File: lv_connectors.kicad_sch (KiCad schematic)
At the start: 18 parts, among them J2 Conn_01x04, J3 Conn_01x04, J4 Conn_01x04, J6 Conn_01x02, J7 Conn_01x04, J8 Conn_01x08, J9 Conn_01x02, U15 ADP121-AUJZ33R7, U2 L7805, U24 SN74LVC1G00DBV

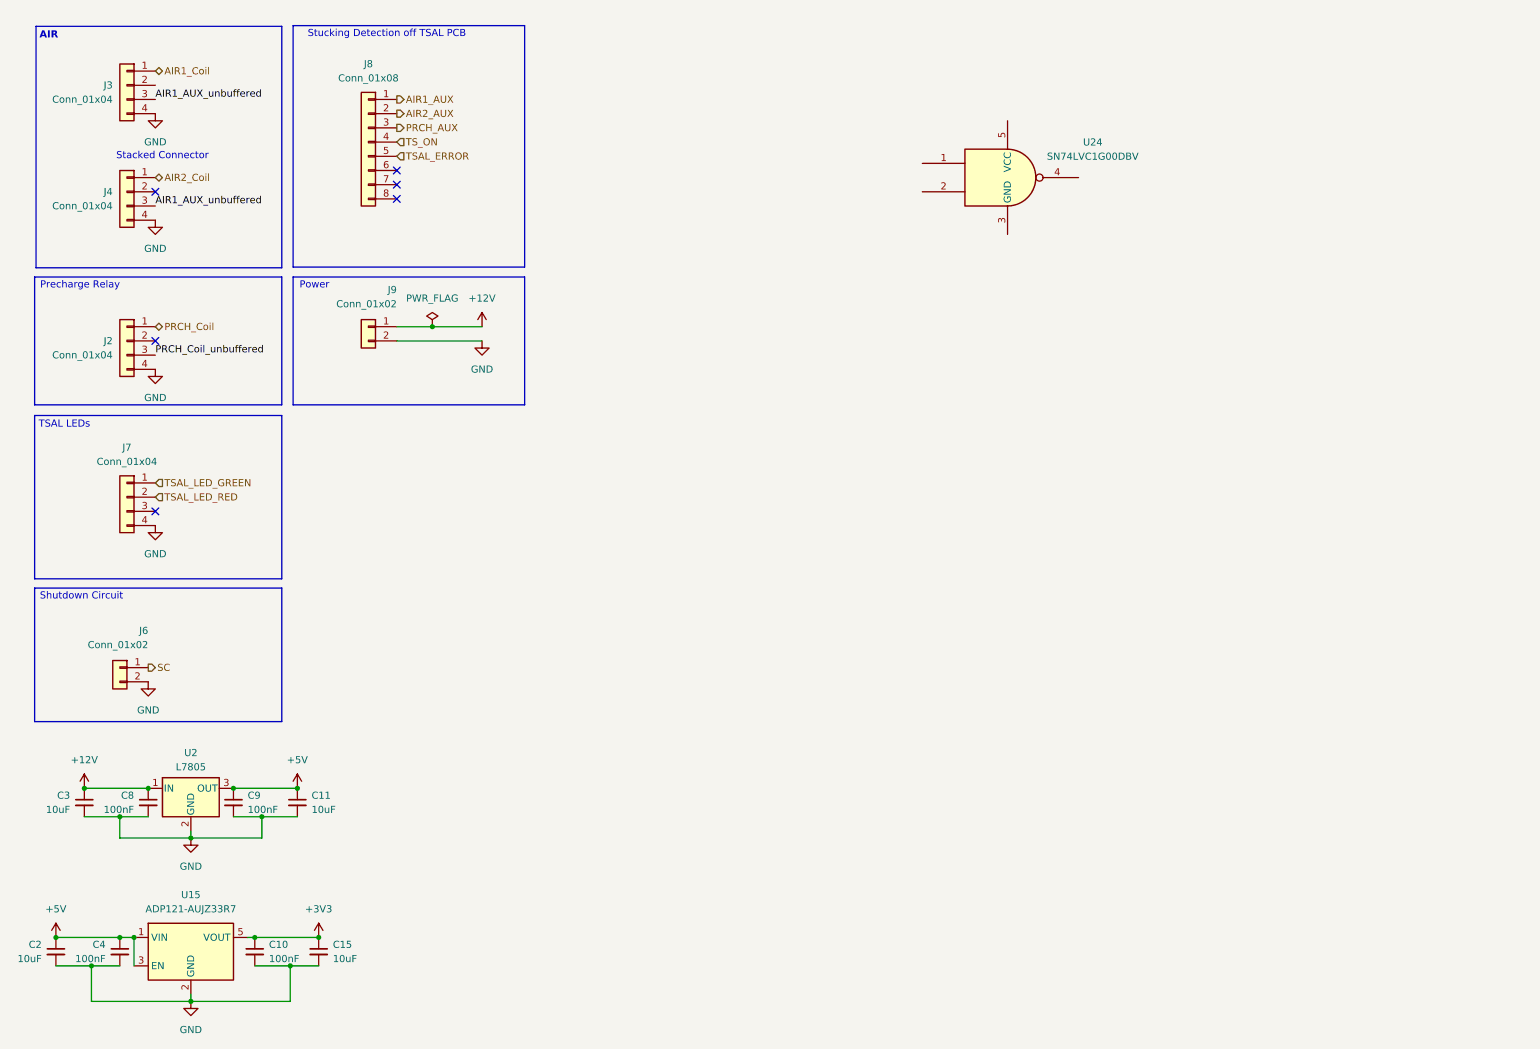
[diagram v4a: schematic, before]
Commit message: Added decoupling Caps
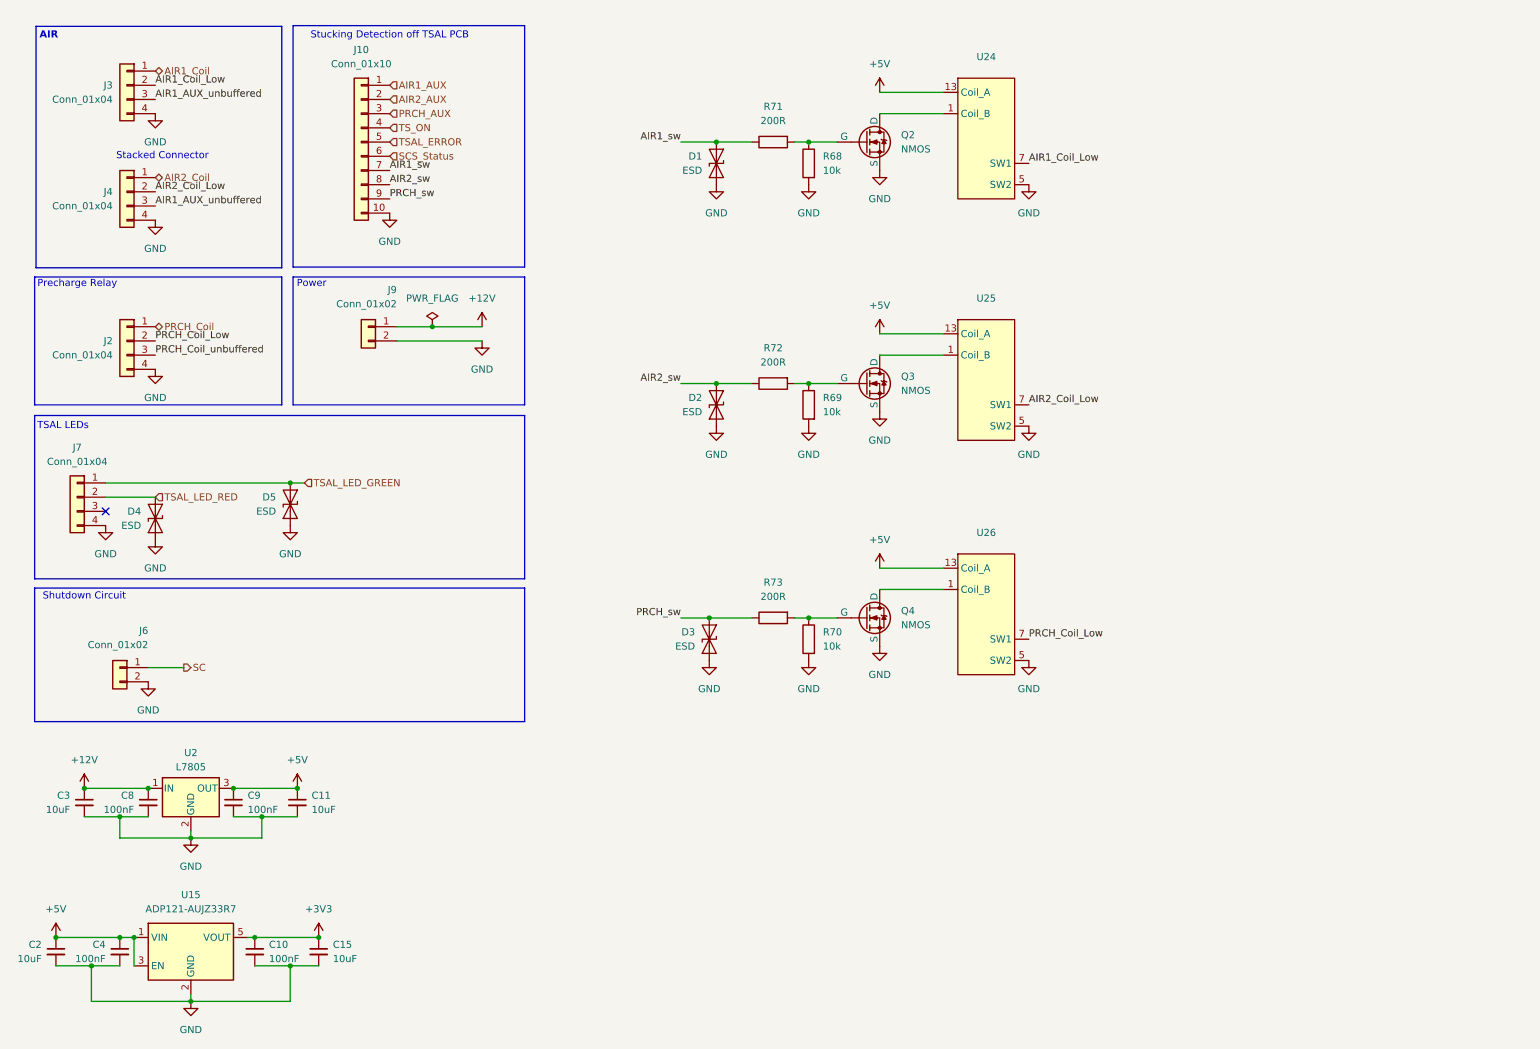
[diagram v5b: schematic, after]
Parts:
- removed J8: Conn_01x08, symbol Connector_Generic:Conn_01x08
- removed U24: SN74LVC1G00DBV, Package_TO_SOT_SMD:SOT-23-5, symbol 74xGxx:SN74LVC1G00DBV
- added D1, D2, D3, D4, D5: ESD, Diode_SMD:Infineon_SG-WLL-2-3_0.58x0.28_P0.36mm, symbol Diode:ESD131-B1-W0201
- added J10: Conn_01x10, symbol Connector_Generic:Conn_01x10
- added Q2, Q3, Q4: NMOS, symbol Simulation_SPICE:NMOS
- added R68, R69, R70: 10k, symbol Device:R
- added R71, R72, R73: 200R, symbol Device:R
- added U24, U25, U26: ~, symbol Zettler:AZ9371
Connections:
- net +5V: now also U24.13 (Coil_A), U25.13 (Coil_A), U26.13 (Coil_A)
- net AIR1_AUX: now also J10.1 (Pin_1)
- net AIR2_AUX: now also J10.2 (Pin_2)
- net GND: now also D1.1 (A1), D2.1 (A1), D3.1 (A1), D4.1 (A1), D5.1 (A1), J10.10 (Pin_10), Q2.3 (S), Q3.3 (S), Q4.3 (S), R68.2, R69.2, R70.2, U24.5 (SW2), U25.5 (SW2), U26.5 (SW2)
- net PRCH_AUX: now also J10.3 (Pin_3)
- net TSAL_ERROR: now also J10.5 (Pin_5)
- net TSAL_LED_GREEN: now also D5.2 (A2)
- net TSAL_LED_RED: now also D4.2 (A2)
- net TS_ON: now also J10.4 (Pin_4)
- net AIR1_Coil_Low: now reaches J3.2 (Pin_2)
- net AIR1_Coil_Low: now also U24.7 (SW1)
- net AIR2_Coil_Low: now reaches J4.2 (Pin_2)
- net AIR2_Coil_Low: now also U25.7 (SW1)
- net PRCH_Coil_Low: now reaches J2.2 (Pin_2)
- net PRCH_Coil_Low: now also U26.7 (SW1)
- new net: Q4.1 (D), U26.1 (Coil_B)
- new net: Q4.2 (G), R70.1, R73.2
- new net: Q3.2 (G), R69.1, R72.2
- new net: Q2.1 (D), U24.1 (Coil_B)
- new net: Q2.2 (G), R68.1, R71.2
- new net: Q3.1 (D), U25.1 (Coil_B)
- new net AIR1_sw: D1.2 (A2), J10.7 (Pin_7), R71.1
- new net AIR2_sw: D2.2 (A2), J10.8 (Pin_8), R72.1
- new net PRCH_sw: D3.2 (A2), J10.9 (Pin_9), R73.1
- new net SCS_Status: J10.6 (Pin_6)
- no-connect marks 6 -> 1
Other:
- moved on the sheet: J7

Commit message: Added Rules
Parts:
- removed C10, C4: 100nF, Capacitor_SMD:C_0603_1608Metric, symbol Device:C_Small
- removed C15, C2: 10uF, Capacitor_SMD:C_0603_1608Metric, symbol Device:C_Small
- removed U15: ADP121-AUJZ33R7, Package_TO_SOT_SMD:TSOT-23-5, symbol Regulator_Linear:ADP7142AUJZ-3.3
- added Q5, Q6: PMOS, symbol Simulation_SPICE:PMOS
- added R78, R79: 200R, symbol Device:R
- added R80, R81: 10k, symbol Device:R
- added R85: 30k, symbol Device:R
- added R86: 7k5, symbol Device:R
- U2: Cost 0,958 -> 0,949; Mouser 511-L7805ACD2T-TR -> 511-L7805ABD2T-TR
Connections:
- net AIR1_Coil_Low is gone; now on net AIR1_Coil: J3.2 (Pin_2), U24.7 (SW1)
- net AIR2_Coil_Low is gone; now on net AIR2_Coil: J4.2 (Pin_2), U25.7 (SW1)
- net PRCH_Coil_Low is gone; now on net PRCH_Coil: J2.2 (Pin_2), U26.7 (SW1)
- net AIR1_AUX_unbuffered: no longer J4.3 (Pin_3)
- net AIR1_Coil: no longer J3.1 (Pin_1)
- net AIR2_Coil: no longer J4.1 (Pin_1)
- net GND: now also R86.2
- net PRCH_Coil: no longer J2.1 (Pin_1)
- net SC: now also R85.2, R86.1; no longer J6.1 (Pin_1)
- net TSAL_LED_GREEN: now also R78.1; no longer D5.2 (A2), J7.1 (Pin_1)
- net TSAL_LED_RED: now also R79.1; no longer D4.2 (A2), J7.2 (Pin_2)
- net +12V renamed +24V
- net +24V: now also Q5.1 (D), Q6.1 (D), R80.1, R81.1
- net PRCH_Coil_unbuffered renamed PRCH_AUX_unbuffered
- new net: Q5.2 (G), R78.2, R81.2
- new net: D4.2 (A2), J7.2 (Pin_2), Q6.3 (S)
- new net: D5.2 (A2), J7.1 (Pin_1), Q5.3 (S)
- new net: Q6.2 (G), R79.2, R80.2
- new net AIR2_AUX_unbuffered: J4.3 (Pin_3)
- new net SDC: J2.1 (Pin_1), J3.1 (Pin_1), J4.1 (Pin_1), J6.1 (Pin_1), R85.1
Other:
- note added: "Stucking Detection off PCB"
- note removed: "Stacked Connector"
- note removed: "Stucking Detection off TSAL PCB"
- moved on the sheet: C11, C3, C8, C9, D1, D2, D3, D5, J10, J6, J7, J9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

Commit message: Submission Ready. ESF 15.07.24
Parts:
- removed D1, D2, D3: ESD, Diode_SMD:Infineon_SG-WLL-2-3_0.58x0.28_P0.36mm, symbol Diode:ESD131-B1-W0201
- removed Q2, Q3, Q4: NMOS, symbol Simulation_SPICE:NMOS
- removed R68, R69, R70: 10k, symbol Device:R
- removed R71, R72, R73: 200R, symbol Device:R
- removed U24, U25, U26: ~, symbol Zettler:AZ9371
- added C1, C10: 100nF, symbol Device:C
- added C15, C4: 10uF, symbol Device:C_Polarized
- added R29, R30, R31: 10k, symbol Device:R
- added U15: TBA1-1211E, Converter_DCDC:Converter_DCDC_TRACO_TBA1-xxxxE_Single_THT, symbol Converter_DCDC:TBA1-1211E
- added U18: IP4252CZ16, Package_SON:Nexperia_HUSON-16_USON-16-1EP_1.35x3.3mm_P0.4mm_EP0.4x2.8mm, symbol Power_Protection:IP4252CZ16
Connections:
- net AIR1_AUX_unbuffered is gone; now on net AIR1_AUX: J3.3 (Pin_3)
- net AIR2_AUX_unbuffered is gone; now on net AIR2_AUX: J4.3 (Pin_3)
- net PRCH_AUX_unbuffered is gone; now on net PRCH_AUX: J2.3 (Pin_3)
- net +24V: now also C1.1, C4.1, U15.1 (+Vin); no longer C3.1, C8.1, U2.1 (IN)
- net +5V: now also R29.1, R30.1, R31.1
- net AIR1_AUX: now also R29.2, U18.16 (CH1); no longer J10.1 (Pin_1)
- net AIR2_AUX: now also R30.2, U18.15 (CH2); no longer J10.2 (Pin_2)
- net GND: now also J10.1 (Pin_1), C1.2, C10.2, C15.2, C4.2, U15.2 (-Vin), U15.4 (-Vout), U18.17 (GND)
- net PRCH_AUX: now also R31.2, U18.14 (CH3); no longer J10.3 (Pin_3)
- net TSAL_ERROR: now also U18.12 (CH5); no longer J10.5 (Pin_5)
- net TS_ON: now also U18.13 (CH4); no longer J10.4 (Pin_4)
- net AIR1_sw: no longer names the net of J10.7 (Pin_7)
- net AIR1_sw: now also U18.6 (CH6)
- net AIR2_sw: no longer names the net of J10.8 (Pin_8)
- net AIR2_sw: now also U18.7 (CH7)
- net PRCH_sw: no longer names the net of J10.9 (Pin_9)
- net PRCH_sw: now also U18.8 (CH8)
- net SCS_Status: no longer names the net of J10.6 (Pin_6)
- net SCS_Status: now also U18.5 (CH5)
- new net: J10.2 (Pin_2), U18.1 (CH1)
- new net: J10.3 (Pin_3), U18.2 (CH2)
- new net: J10.4 (Pin_4), U18.3 (CH3)
- new net: J10.5 (Pin_5), U18.4 (CH4)
- new net +9V: C10.1, C15.1, C3.1, C8.1, U15.6 (+Vout), U2.1 (IN)
- new net AIR1_SW: U18.11 (CH6)
- new net AIR2_SW: U18.10 (CH7)
- new net PRCH_SW: U18.9 (CH8)
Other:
- note added: "5V Supply"
- note added: "DC-DC Converter"
- note added: "Power In"
- note removed: "Power"
- moved on the sheet: C11, C3, C8, C9, D4, D5, J10, J2, J3, J4, J6, J7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

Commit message: ⠀⠀⠀⠀⠀⠀⠀⠀⠀⠀⠀⠀⠀⠀⠀⠀⠀⠀⠀⠀⠀⠀⠀⠀⠀⠀⠀⠀⠀⠀⠀⠀⠀⠀⠀⠀⠀⣠⣤⣤⣤⡀⠀⠀⠀⠀⠀⠀⠀⠀⠀⠀⠀⠀⠀⠀⠀⠀⠀⠀⠀⠀⠀⠀⠀ ⠀⠀⠀⠀⠀⠀⠀⠀⠀⠀⠀⠀⠀⠀⠀⠀⠀⠀⠀⠀⠀⠀⠀⠀⠀⠀⠀⠀⠀⠀⠀⠀⠀⠀⣠⣶⣿⠟⠉⠉⠻⣿⡄⠀⠀⠀⠀⠀⠀⠀⠀⠀⠀⠀⠀⠀⠀⠀⠀⠀⠀⠀⠀⠀⠀ ⠀⠀⠀⠀⠀⠀⠀⠀⠀⠀⠀⠀⠀⠀⠀⠀⠀⠀⠀⠀⠀⠀⠀⠀⠀⠀⠀⠀⠀⠀⠀⢀⣤⣾⠿⠉⠀⠀⠀⠀⠀⠹⣿⡄⠀⠀⠀⠀⠀⠀⠀⠀⠀⠀⠀⠀⠀⠀⠀⠀⠀⠀⣀⣴⣾ ⠀⠀⠀⠀⠀⠀⠀⠀⠀⠀⠀⠀⠀⠀⠀⠀⠀⠀⠀⠀⠀⠀⠀⠀⠀⠀⠀⠀⠀⢀⣴⣿⠟⠁⠀⠀⠀⠀⠀⠀⠀⠀⣿⣿⠀⠀⠀⠀⠀⠀⠀⠀⠀⠀⠀⠀⠀⠀⠀⣀⣴⣾⡿⠛⠉ ⠀⠀⠀⠀⠀⠀⠀⠀⠀⠀⠀⠀⠀⠀⠀⠀⠀⠀⠀⠀⠀⠀⠀⠀⠀⠀⠀⢀⣴⣿⠟⠁⠀⠀⠀⠀⠀⠀⠀⠀⠀⠀⢸⣿⡆⠀⠀⠀⠀⠀⠀⠀⠀⠀⠀⠀⢀⣴⣾⡿⠟⠁⠀⠀⠀ ⠀⠀⠀⠀⠀⠀⠀⠀⠀⠀⠀⠀⠀⠀⠀⠀⠀⠀⠀⠀⠀⠀⠀⠀⢀⣀⣴⣿⡿⠃⠀⠀⠀⠀⠀⠀⠀⠀⠀⠀⠀⠀⢸⣿⣷⣶⣶⣦⣤⣤⣄⡀⠀⢀⣠⣾⣿⠿⠋⠀⠀⠀⠀⠀⣠ ⠀⠀⠀⠀⠀⠀⠀⠀⠀⠀⠀⠀⠀⠀⠀⠀⠀⠀⠀⠀⠀⠀⠀⣼⣿⣿⡿⠋⠀⠀⠀⠀⠀⠀⠀⠀⠀⠀⠀⣠⣤⠶⠞⣿⠟⠋⠉⠉⠙⣻⠿⢿⣿⣿⣿⠟⠁⠀⠀⠀⠀⠀⢀⡼⠁ ⠀⠀⠀⠀⠀⠀⠀⠀⠀⠀⠀⠀⠀⠀⠀⠀⠀⠀⠀⠀⠀⠀⢰⣿⠁⠛⠀⠀⠀⠀⠀⠀⠀⠀⠀⠀⠀⠀⣰⠟⠁⢠⡞⠁⠀⠀⠀⢀⡴⠋⠀⢀⡿⠋⠁⠀⠀⠀⠀⠀⠀⠀⡞⠁⠀ ⠀⠀⠀⠀⠀⠀⠀⠀⠀⠀⠀⠀⠀⠀⠀⠀⠀⠀⠀⠀⠀⣠⣼⣿⡄⠀⠀⠀⠀⠀⠀⠀⠀⠀⠀⠀⠀⣼⠃⠀⢠⠏⠀⠀⠀⠀⣰⠏⠀⠀⣠⠟⠀⠀⠀⠀⠀⠀⠀⠀⠀⢸⡥⠤⡀ ⠀⠀⠀⠀⠀⠀⠀⠀⠀⠀⠀⠀⠀⠀⠀⠀⠀⠀⠀⠀⣰⣿⠟⠁⠀⠀⠀⠀⠀⠀⠀⠀⠀⠀⠀⠀⠠⣇⠀⣠⡏⠀⠀⠀⠀⣼⠁⠀⠀⣰⠋⠀⠀⠀⠀⠀⠀⠀⠀⠀⠀⠀⢀⡴⠁ ⠀⠀⠀⠀⠀⠀⠀⠀⠀⠀⠀⠀⠀⠀⠀⠀⣀⣄⣄⣼⣿⠋⠀⠀⠀⠀⠀⠀⠀⠀⠀⠀⠀⠀⠀⠀⠀⢻⡶⠋⠀⠀⠀⠀⢸⣧⠀⠀⣴⠃⠀⠀⠀⠀⠀⠀⠀⠀⠀⠀⠀⠀⠘⢧⠀ ⠀⠀⠀⠀⠀⠀⠀⠀⢀⣀⣀⠀⠀⠀⠀⣾⡿⠿⣿⡿⠁⠀⠀⠀⠀⠀⠀⣠⣶⣶⣶⡀⠀⠀⠀⠀⠀⠀⠀⠀⠀⠀⠀⠀⠀⠙⠛⠛⠁⠀⠀⠀⠀⠀⠀⠀⠀⠀⠀⠀⠀⠀⠀⠈⠳ ⠀⠀⠀⠀⠀⠀⢀⣾⠿⠛⢿⣿⣷⣄⡀⣿⠃⠀⠈⠀⠀⠀⠀⠀⠀⢀⣾⣿⣿⣿⣿⣧⠀⠀⠀⠀⠀⠀⠀⠀⠀⠀⠀⠀⠀⠀⠀⠀⠀⠀⠀⠀⠀⠀⠀⠀⠀⠀⠀⠀⠀⠀⠀⠀⠀ ⠀⠀⠀⣠⣤⣦⣼⣿⠀⠀⠀⣿⣿⣿⣿⣿⣦⣀⠀⠀⠀⠀⠀⠀⠀⣿⣿⣿⣿⣿⣿⡿⠀⠀⠀⢀⣀⣀⣀⣀⡀⠀⠀⠀⠀⠀⠀⠀⠀⠀⠀⣤⣾⣿⣿⣿⣷⣄⠀⠀⠀⠀⠀⠀⠀ ⠀⣠⣾⡿⠋⠉⠉⠁⠀⠀⠀⠀⠉⢯⡙⠻⣿⣿⣷⣤⡀⠀⠀⠀⠀⢿⣿⣿⣿⣿⡿⠃⢀⡤⠖⠋⠉⠉⠉⠉⠉⠉⠒⠦⣄⠀⠀⠀⠀⠀⣾⣿⣿⣿⣿⣿⣿⣿⣧⠀⠀⠀⠀⠀⠀ ⣾⣿⠋⠀⠀⠀⠀⣀⣀⠀⠀⠀⠀⠀⠙⢦⣄⠉⠻⢿⣿⣷⣦⡀⠀⠈⠙⠛⠛⠋⠀⢰⠟⡇⠀⠀⠀⠀⠀⠀⠀⠀⠀⠀⠈⠳⣄⠀⠀⠀⣿⣿⣿⣿⣿⣿⣿⣿⣿⠀⠀⠀⠀⠀⠀ ⣿⡇⠀⠀⠀⣴⠟⣫⣿⣿⣄⠀⠀⠀⠀⡶⢌⡙⠶⣤⡈⠛⠿⣿⣷⣦⣀⠀⠀⠀⠀⡇⠀⢻⣄⠀⠀⣠⢷⠀⠀⠀⠀⠀⡶⠀⠘⡆⠀⠀⠻⣿⣿⣿⣿⣿⣿⣿⡟⠀⠀⠀⠀⠀⠀ ⣿⡇⠀⠀⢸⣟⢸⣿⣿⣿⣿⠀⠀⠀⠀⡇⠀⠈⠛⠦⣝⡳⢤⣈⠛⠻⣿⣷⣦⣀⠀⠀⠀⠀⠈⠙⠋⠁⠀⠛⠦⠤⠤⠚⠁⠀⠀⢳⠀⠀⠀⠈⠛⠿⠿⠿⠟⠋⠀⠀⠀⠀⠀⠀⠀ ⣿⡇⠀⠀⠈⢿⣞⣿⣿⣿⠏⠀⠀⠀⠀⡇⠀⠀⠀⠀⠀⠙⠳⢬⣛⠦⠀⠙⢻⣿⣷⣦⣀⠀⠀⠀⠀⠀⠀⠀⠀⠀⠀⠀⠀⠀⠀⡞⠀⠀⠀⠀⠀⠀⠀⠀⠀⠀⠀⠀⠀⠀⠀⠀⠀ ⣿⡇⠀⠀⠀⠀⠉⠛⠋⠁⠀⠀⠀⠀⠀⡇⠀⠀⠀⠀⠀⠀⠀⠀⠈⠁⠀⠀⠈⣿⠉⢻⣿⣷⣦⣀⠀⠀⠀⠀⠀⠀⠀⠀⠀⢀⡼⠁⠀⠀⠀⠀⠀⠀⠀⠀⠀⠀⠀⠀⠀⠀⠀⠀⠀ ⣿⡇⠀⠀⠀⠀⠀⣠⣄⠀⠀⢰⠶⠒⠒⢧⣄⡀⠀⠀⠀⠀⠀⠀⠀⠀⠀⠀⠀⣿⠀⢸⡇⢸⡟⢿⣷⣦⣴⣶⣶⣶⣶⣤⣔⠋⠀⠀⠀⠀⠀⠀⠀⠀⠀⠀⠀⠀⠀⠀⠀⠀⠀⠀⠀ ⣿⡇⠀⠀⣤⠀⠀⠿⠿⠁⢀⡿⠀⠀⠀⡄⠈⠙⡷⢦⣄⡀⠀⠀⠀⠀⠀⠀⠀⣿⠀⢸⡇⢸⡇⠀⣿⠙⣿⣿⣉⠉⠙⠿⣿⣧⠀⠀⠀⠀⠀⠀⠀⠀⠀⠀⠀⠀⠀⠀⠀⠀⠀⠀⠀ ⣿⡇⠀⠀⠙⠷⢤⣀⣠⠴⠛⠁⠀⠀⠀⠇⠀⠀⡇⢸⡏⢹⡷⢦⣄⡀⠀⠀⠀⣿⡀⢸⡇⢸⡇⠀⡟⠀⢸⠀⢹⡷⢦⣄⣘⣿⡆⠀⠀⠀⠀⠀⠀⠀⠀⠀⠀⠀⠀⠀⠀⠀⠀⠀⠀ ⣿⣿⠢⣤⡀⠀⠀⠀⠀⠀⠀⣠⠾⣿⣿⡷⣤⣀⡇⠸⡇⢸⡇⢸⠉⠙⠳⢦⣄⡻⢿⣾⣧⣸⣧⠀⡇⠀⢸⠀⢸⡇⢤⣈⠙⠻⣿⣆⠀⠀⠀⠀⠀⠀⠀⠀⠀⠀⠀⠀⠀⠀⠀⠀⠀ ⢹⣿⣷⣌⡉⠛⠲⢶⣶⠖⠛⠛⢶⣄⡉⠛⠿⣽⣿⣶⣧⣸⡇⢸⠀⠀⠀⠀⠈⠙⠲⢮⣝⠻⣿⣷⣷⣄⣸⠀⢸⡇⠀⠈⠁⠀⢸⣿⠀⠀⠀⠀⠀⠀⠀⠀⠀⠀⠀⠀⠀⠀⠀⠀⠀ ⠀⠈⠙⠻⢿⣷⣶⣤⣉⡻⢶⣄⣀⠈⠙⠳⢦⣈⡉⠻⢿⣿⣷⣾⣦⡀⠀⠀⠀⠀⠀⠀⠈⠙⠲⢭⣛⠿⣿⣷⣼⡇⠀⠀⠀⠀⠈⣿⡇⠀⠀⠀⠀⠀⠀⣀⠀⠀⠀⠀⠀⠀⠀⠀⣀ ⠀⠀⠀⠀⠀⠈⠙⠻⢿⣿⣷⣶⣽⣻⡦⠀⠀⠈⠙⠷⣦⣌⡙⠻⢿⣟⣷⣤⣀⠀⠀⠀⠀⠀⠀⠀⠈⠙⠳⢯⣻⡇⠀⠀⠀⠀⠀⢸⣿⠀⣀⠀⠀⠀⠀⠈⠳⣄⠀⠀⠀⢀⡏⠙⠛ ⠀⠀⠀⠀⠀⠀⠀⠀⠀⠈⠛⠻⢿⣿⣿⣿⣶⣤⣤⣤⣀⣈⠛⠷⣤⣈⡛⠷⢽⡻⢶⣄⣀⠀⠀⠀⠀⠀⠀⠀⠈⠛⠳⢤⣀⠀⠀⢸⣿⡀⠈⠳⢤⣀⣀⣰⠃⠈⠛⠶⠶⠿⠃⠀⠀ ⠀⠀⠀⠀⠀⠀⠀⠀⠀⠀⠀⠀⠀⢈⣿⡿⠛⠉⠙⠛⠛⠻⢷⣦⣄⣩⣿⠶⠖⠛⠛⠛⠛⠛⠛⠿⢷⣶⣦⣄⠀⠀⠀⠀⠉⢻⣶⣿⣿⠇⠀⠀⠀⠉⠉⠀⠀⠀⠀⠀⠀⠀⠀⠀⠀ ⠀⠀⠀⠀⠀⠀⠀⠀⠀⠀⠀⠀⠀⣼⣿⠁⠀⠀⠀⠀⠀⠀⠀⣿⣿⠋⠀⠀⠀⠀⠀⣠⠖⠂⠀⠀⠀⠈⠙⠿⣿⣦⡄⠀⠀⣸⣿⠟⠋⠀⠀⠀⠀⠀⠀⠀⠀⠀⠀⠀⠀⠀⠀⠀⠀ ⠀⠀⠀⠀⠀⠀⠀⠀⠀⠀⠀⠀⢰⣿⡟⠀⠀⠀⠀⠀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
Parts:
- C1, C10, C15, C4: footprint (none) -> Capacitor_SMD:C_0603_1608Metric
- Q5, Q6: footprint (none) -> Package_TO_SOT_SMD:SOT-23-3
- R29, R30, R31, R78, R79, R80, R81, R85, R86: footprint (none) -> Resistor_SMD:R_0603_1608Metric
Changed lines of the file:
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@@
 			)
 		)
-		(property "Footprint" ""
+		(property "Footprint" "Resistor_SMD:R_0603_1608Metric"
 			(at 80.01 144.018 90)
 			(effects
@@
 			)
 		)
-		(property "Footprint" ""
+		(property "Footprint" "Package_TO_SOT_SMD:SOT-23-3"
 			(at 58.42 170.18 0)
 			(effects
@@
 			)
 		)
+		(property "resistor datasheet" ""
+			(at 63.5 172.72 0)
+			(effects
+				(font
+					(size 1.27 1.27)
+				)
+			)
+		)
 		(pin "1"
 		)
@@
 			)
 		)
-		(property "Footprint" ""
+		(property "Footprint" "Resistor_SMD:R_0603_1608Metric"
 			(at 70.612 137.16 90)
 			(effects
@@
 			)
 		)
-		(property "Footprint" ""
+		(property "Footprint" "Capacitor_SMD:C_0603_1608Metric"
 			(at 218.7448 43.18 0)
 			(effects
@@
 			)
 		)
-		(property "Footprint" ""
+		(property "Footprint" "Capacitor_SMD:C_0603_1608Metric"
 			(at 206.0448 43.18 0)
 			(effects
@@
 			)
 		)
-		(property "Footprint" ""
+		(property "Footprint" "Resistor_SMD:R_0603_1608Metric"
 			(at 80.01 174.498 90)
 			(effects
@@
 			)
 		)
-		(property "Footprint" ""
+		(property "Footprint" "Resistor_SMD:R_0603_1608Metric"
 			(at 41.402 44.45 90)
 			(effects
@@
 			)
 		)
-		(property "Footprint" ""
+		(property "Footprint" "Capacitor_SMD:C_0603_1608Metric"
 			(at 258.7752 43.18 0)
 			(effects
@@
 			)
 		)
-		(property "Footprint" ""
+		(property "Footprint" "Resistor_SMD:R_0603_1608Metric"
 			(at 41.402 24.13 90)
 			(effects
@@
 			)
 		)
-		(property "Footprint" ""
+		(property "Footprint" "Resistor_SMD:R_0603_1608Metric"
 			(at 57.912 100.33 90)
 			(effects
@@
 			)
 		)
-		(property "Footprint" ""
+		(property "Footprint" "Resistor_SMD:R_0603_1608Metric"
 			(at 57.912 110.49 90)
 			(effects
@@
 			)
 		)
-		(property "Footprint" ""
+		(property "Footprint" "Package_TO_SOT_SMD:SOT-23-3"
 			(at 58.42 139.7 0)
 			(effects
@@
 			)
 		)
-		(property "Footprint" ""
+		(property "Footprint" "Capacitor_SMD:C_0603_1608Metric"
 			(at 271.4752 43.18 0)
 			(effects
@@
 			)
 		)
-		(property "Footprint" ""
+		(property "Footprint" "Resistor_SMD:R_0603_1608Metric"
 			(at 41.402 68.58 90)
 			(effects
@@
 			)
 		)
-		(property "Footprint" ""
+		(property "Footprint" "Resistor_SMD:R_0603_1608Metric"
 			(at 70.612 167.64 90)
 			(effects
